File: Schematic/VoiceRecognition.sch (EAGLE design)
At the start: 26 parts, among them Q1 16MHz, X1 USB-A

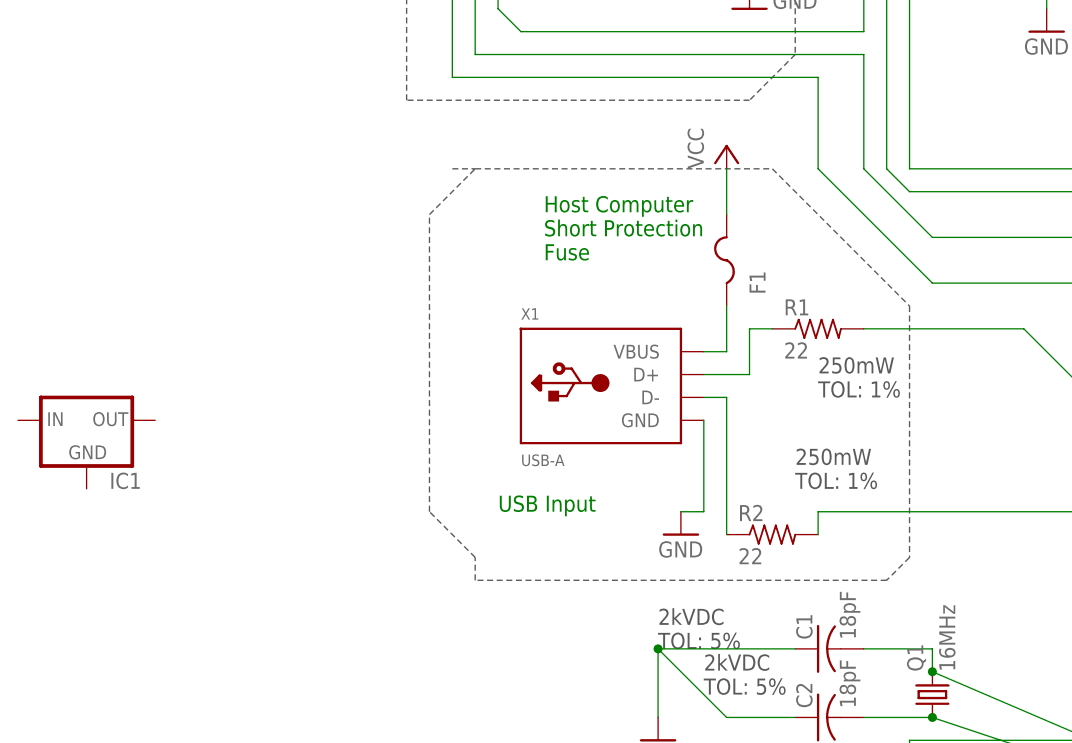
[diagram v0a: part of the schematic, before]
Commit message: Added some EagleCAD schematic updates
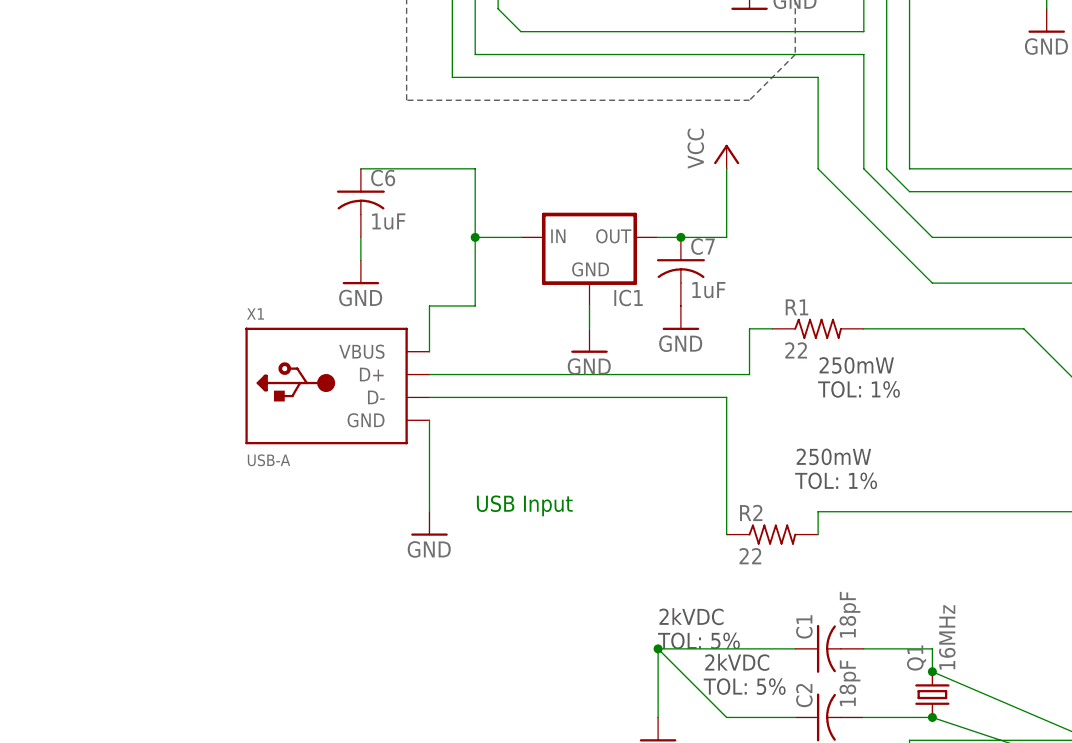
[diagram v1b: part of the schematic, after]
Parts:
- removed F1: (no value), adafruit:PTCFUSE-1206
- added C6, C7: 1uF, rcl:C-USC1206
- IC1: VENDOR (none) -> Mouser; VPN (none) -> 579-MCP1700-5002E/TO
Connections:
- net GND: now also C6.2, C7.2, IC1.GND
- net N$10: now also C6.1, IC1.IN; no longer F1.1
- net VCC: now also C7.1, IC1.OUT; no longer F1.2
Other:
- note removed: "Host Computer Short Protection Fuse"
- moved on the sheet: IC1, X1
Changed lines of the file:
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@@
 <part name="C5" library="rcl" library_urn="urn:adsk.eagle:library:334" deviceset="C-US" device="C1206" package3d_urn="urn:adsk.eagle:package:23618/2" value="10uF"/>
 <part name="GND10" library="supply1" library_urn="urn:adsk.eagle:library:371" deviceset="GND" device=""/>
-<part name="F1" library="adafruit" deviceset="PTCFUSE" device="-1206"/>
 <part name="GND11" library="supply1" library_urn="urn:adsk.eagle:library:371" deviceset="GND" device=""/>
 <part name="JP2" library="pinhead" library_urn="urn:adsk.eagle:library:325" deviceset="PINHD-1X3" device="" package3d_urn="urn:adsk.eagle:package:22458/2"/>
@@
 <part name="P+1" library="supply1" library_urn="urn:adsk.eagle:library:371" deviceset="VCC" device=""/>
 <part name="GND14" library="supply1" library_urn="urn:adsk.eagle:library:371" deviceset="GND" device=""/>
-<part name="IC1" library="adafruit" deviceset="MCP1700" device="INLINE"/>
+<part name="IC1" library="adafruit" deviceset="MCP1700" device="INLINE">
+<attribute name="VENDOR" value="Mouser"/>
+<attribute name="VPN" value=" 579-MCP1700-5002E/TO "/>
+</part>
+<part name="C6" library="rcl" library_urn="urn:adsk.eagle:library:334" deviceset="C-US" device="C1206" package3d_urn="urn:adsk.eagle:package:23618/2" value="1uF"/>
+<part name="GND15" library="supply1" library_urn="urn:adsk.eagle:library:371" deviceset="GND" device=""/>
+<part name="GND16" library="supply1" library_urn="urn:adsk.eagle:library:371" deviceset="GND" device=""/>
+<part name="C7" library="rcl" library_urn="urn:adsk.eagle:library:334" deviceset="C-US" device="C1206" package3d_urn="urn:adsk.eagle:package:23618/2" value="1uF"/>
+<part name="GND17" library="supply1" library_urn="urn:adsk.eagle:library:371" deviceset="GND" device=""/>
 </parts>
 <sheets>
@@
 <text x="88.9" y="175.26" size="1.778" layer="91">ICSP Input</text>
 <text x="236.22" y="177.8" size="1.778" layer="91">Visual Indicators</text>
-<text x="86.36" y="129.54" size="1.778" layer="91">Host Computer
-Short Protection
-Fuse</text>
-<text x="81.28" y="101.6" size="1.778" layer="91">USB Input</text>
+<text x="78.74" y="101.6" size="1.778" layer="91">USB Input</text>
 <text x="86.36" y="53.34" size="1.778" layer="91">Audio Input from Microphone Daughter Board</text>
 <text x="38.1" y="165.1" size="1.778" layer="91">ECE411 Group 3
@@
 <wire x1="71.12" y1="147.32" x2="71.12" y2="177.8" width="0.1524" layer="97" style="shortdash"/>
 <wire x1="71.12" y1="177.8" x2="76.2" y2="182.88" width="0.1524" layer="97" style="shortdash"/>
-<wire x1="76.2" y1="139.7" x2="78.74" y2="139.7" width="0.1524" layer="97" style="shortdash"/>
-<wire x1="78.74" y1="139.7" x2="111.76" y2="139.7" width="0.1524" layer="97" style="shortdash"/>
-<wire x1="111.76" y1="139.7" x2="127" y2="124.46" width="0.1524" layer="97" style="shortdash"/>
-<wire x1="127" y1="124.46" x2="127" y2="96.52" width="0.1524" layer="97" style="shortdash"/>
-<wire x1="127" y1="96.52" x2="124.46" y2="93.98" width="0.1524" layer="97" style="shortdash"/>
-<wire x1="124.46" y1="93.98" x2="78.74" y2="93.98" width="0.1524" layer="97" style="shortdash"/>
-<wire x1="78.74" y1="93.98" x2="78.74" y2="96.52" width="0.1524" layer="97" style="shortdash"/>
-<wire x1="78.74" y1="96.52" x2="73.66" y2="101.6" width="0.1524" layer="97" style="shortdash"/>
-<wire x1="73.66" y1="101.6" x2="73.66" y2="134.62" width="0.1524" layer="97" style="shortdash"/>
-<wire x1="73.66" y1="134.62" x2="78.74" y2="139.7" width="0.1524" layer="97" style="shortdash"/>
 <wire x1="83.82" y1="58.42" x2="134.62" y2="58.42" width="0.1524" layer="97" style="shortdash"/>
 <wire x1="134.62" y1="58.42" x2="142.24" y2="50.8" width="0.1524" layer="97" style="shortdash"/>
@@
 <attribute name="VALUE" x="175.26" y="111.76" size="1.778" layer="96"/>
 </instance>
-<instance part="X1" gate="G$1" x="93.98" y="114.3" smashed="yes">
-<attribute name="NAME" x="83.82" y="122.936" size="1.27" layer="95"/>
-<attribute name="VALUE" x="83.82" y="106.68" size="1.27" layer="96"/>
+<instance part="X1" gate="G$1" x="63.5" y="114.3" smashed="yes">
+<attribute name="NAME" x="53.34" y="122.936" size="1.27" layer="95"/>
+<attribute name="VALUE" x="53.34" y="106.68" size="1.27" layer="96"/>
 </instance>
 <instance part="R1" gate="G$1" x="116.84" y="121.92" smashed="yes">
@@
 <attribute name="VALUE" x="176.276" y="158.369" size="1.778" layer="96"/>
 </instance>
-<instance part="GND10" gate="1" x="101.6" y="99.06" smashed="yes">
-<attribute name="VALUE" x="99.06" y="96.52" size="1.778" layer="96"/>
-</instance>
-<instance part="F1" gate="G$1" x="104.14" y="129.54" smashed="yes" rot="MR90">
-<attribute name="VALUE" x="102.87" y="125.73" size="1.778" layer="96" rot="MR90"/>
-<attribute name="NAME" x="109.22" y="125.73" size="1.778" layer="95" rot="MR90"/>
+<instance part="GND10" gate="1" x="73.66" y="99.06" smashed="yes">
+<attribute name="VALUE" x="71.12" y="96.52" size="1.778" layer="96"/>
 </instance>
 <instance part="GND11" gate="1" x="109.22" y="157.48" smashed="yes">
@@
 <attribute name="VALUE" x="248.92" y="48.26" size="1.778" layer="96"/>
 </instance>
-<instance part="IC1" gate="1" x="35.56" y="111.76" smashed="yes">
-<attribute name="NAME" x="38.1" y="104.14" size="1.778" layer="95"/>
-<attribute name="VALUE" x="38.1" y="101.6" size="1.778" layer="96"/>
+<instance part="IC1" gate="1" x="91.44" y="132.08" smashed="yes">
+<attribute name="NAME" x="93.98" y="124.46" size="1.778" layer="95"/>
+<attribute name="VALUE" x="93.98" y="121.92" size="1.778" layer="96"/>
+<attribute name="VENDOR" x="91.44" y="132.08" size="1.778" layer="96" display="off"/>
+<attribute name="VPN" x="91.44" y="132.08" size="1.778" layer="96" display="off"/>
+</instance>
+<instance part="C6" gate="G$1" x="66.04" y="137.16" smashed="yes">
+<attribute name="NAME" x="67.056" y="137.795" size="1.778" layer="95"/>
+<attribute name="VALUE" x="67.056" y="132.969" size="1.778" layer="96"/>
+</instance>
+<instance part="GND15" gate="1" x="66.04" y="127" smashed="yes">
+<attribute name="VALUE" x="63.5" y="124.46" size="1.778" layer="96"/>
+</instance>
+<instance part="GND16" gate="1" x="91.44" y="119.38" smashed="yes">
+<attribute name="VALUE" x="88.9" y="116.84" size="1.778" layer="96"/>
+</instance>
+<instance part="C7" gate="G$1" x="101.6" y="129.54" smashed="yes">
+<attribute name="NAME" x="102.616" y="130.175" size="1.778" layer="95"/>
+<attribute name="VALUE" x="102.616" y="125.349" size="1.778" layer="96"/>
+</instance>
+<instance part="GND17" gate="1" x="101.6" y="121.92" smashed="yes">
+<attribute name="VALUE" x="99.06" y="119.38" size="1.778" layer="96"/>
 </instance>
 </instances>
@@
 <segment>
 <pinref part="X1" gate="G$1" pin="GND"/>
-<wire x1="104.14" y1="111.76" x2="104.14" y2="101.6" width="0.1524" layer="91"/>
 <pinref part="GND10" gate="1" pin="GND"/>
-<wire x1="104.14" y1="101.6" x2="101.6" y2="101.6" width="0.1524" layer="91"/>
+<wire x1="73.66" y1="111.76" x2="73.66" y2="101.6" width="0.1524" layer="91"/>
 </segment>
 <segment>
@@
 <wire x1="251.46" y1="53.34" x2="251.46" y2="60.96" width="0.1524" layer="91"/>
 </segment>
+<segment>
+<pinref part="C6" gate="G$1" pin="2"/>
+<wire x1="66.04" y1="132.08" x2="66.04" y2="129.54" width="0.1524" layer="91"/>
+<pinref part="GND15" gate="1" pin="GND"/>
+</segment>
+<segment>
+<pinref part="IC1" gate="1" pin="GND"/>
+<pinref part="GND16" gate="1" pin="GND"/>
+<wire x1="91.44" y1="124.46" x2="91.44" y2="121.92" width="0.1524" layer="91"/>
+</segment>
+<segment>
+<pinref part="C7" gate="G$1" pin="2"/>
+<pinref part="GND17" gate="1" pin="GND"/>
+</segment>
 </net>
 <net name="N$6" class="0">
@@
 <wire x1="109.22" y1="121.92" x2="109.22" y2="116.84" width="0.1524" layer="91"/>
 <pinref part="X1" gate="G$1" pin="D+"/>
-<wire x1="109.22" y1="116.84" x2="104.14" y2="116.84" width="0.1524" layer="91"/>
+<wire x1="109.22" y1="116.84" x2="73.66" y2="116.84" width="0.1524" layer="91"/>
 </segment>
 </net>
@@
 <segment>
 <pinref part="X1" gate="G$1" pin="D-"/>
-<wire x1="104.14" y1="114.3" x2="106.68" y2="114.3" width="0.1524" layer="91"/>
+<wire x1="73.66" y1="114.3" x2="106.68" y2="114.3" width="0.1524" layer="91"/>
 <pinref part="R2" gate="G$1" pin="1"/>
 <wire x1="106.68" y1="114.3" x2="106.68" y2="99.06" width="0.1524" layer="91"/>
@@
 <segment>
 <pinref part="X1" gate="G$1" pin="VBUS"/>
-<wire x1="104.14" y1="119.38" x2="106.68" y2="119.38" width="0.1524" layer="91"/>
-<pinref part="F1" gate="G$1" pin="1"/>
-<wire x1="106.68" y1="124.46" x2="106.68" y2="119.38" width="0.1524" layer="91"/>
+<wire x1="73.66" y1="119.38" x2="73.66" y2="124.46" width="0.1524" layer="91"/>
+<wire x1="78.74" y1="124.46" x2="73.66" y2="124.46" width="0.1524" layer="91"/>
+<wire x1="78.74" y1="124.46" x2="78.74" y2="132.08" width="0.1524" layer="91"/>
+<pinref part="IC1" gate="1" pin="IN"/>
+<wire x1="78.74" y1="132.08" x2="83.82" y2="132.08" width="0.1524" layer="91"/>
+<wire x1="78.74" y1="132.08" x2="78.74" y2="139.7" width="0.1524" layer="91"/>
+<junction x="78.74" y="132.08"/>
+<pinref part="C6" gate="G$1" pin="1"/>
+<wire x1="78.74" y1="139.7" x2="66.04" y2="139.7" width="0.1524" layer="91"/>
 </segment>
 </net>
@@
 <wire x1="220.98" y1="167.64" x2="228.6" y2="167.64" width="0.1524" layer="91"/>
 <pinref part="P+10" gate="VCC" pin="VCC"/>
-</segment>
-<segment>
-<pinref part="F1" gate="G$1" pin="2"/>
-<wire x1="106.68" y1="134.62" x2="106.68" y2="139.7" width="0.1524" layer="91"/>
-<pinref part="P+11" gate="VCC" pin="VCC"/>
 </segment>
 <segment>
@@
 <wire x1="256.54" y1="68.58" x2="256.54" y2="60.96" width="0.1524" layer="91"/>
 </segment>
-</net>
+<segment>
+<pinref part="IC1" gate="1" pin="OUT"/>
+<wire x1="99.06" y1="132.08" x2="101.6" y2="132.08" width="0.1524" layer="91"/>
+<pinref part="P+11" gate="VCC" pin="VCC"/>
+<wire x1="101.6" y1="132.08" x2="106.68" y2="132.08" width="0.1524" layer="91"/>
+<wire x1="106.68" y1="132.08" x2="106.68" y2="139.7" width="0.1524" layer="91"/>
+<pinref part="C7" gate="G$1" pin="1"/>
+<junction x="101.6" y="132.08"/>
+</segment>
+</net>
